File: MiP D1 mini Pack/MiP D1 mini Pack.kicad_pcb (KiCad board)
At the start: 2 copper layers, 41.4 x 63.8 mm, 12 parts, among them J1 MiP, J2 Debug, U1 WEMOS D1 mini

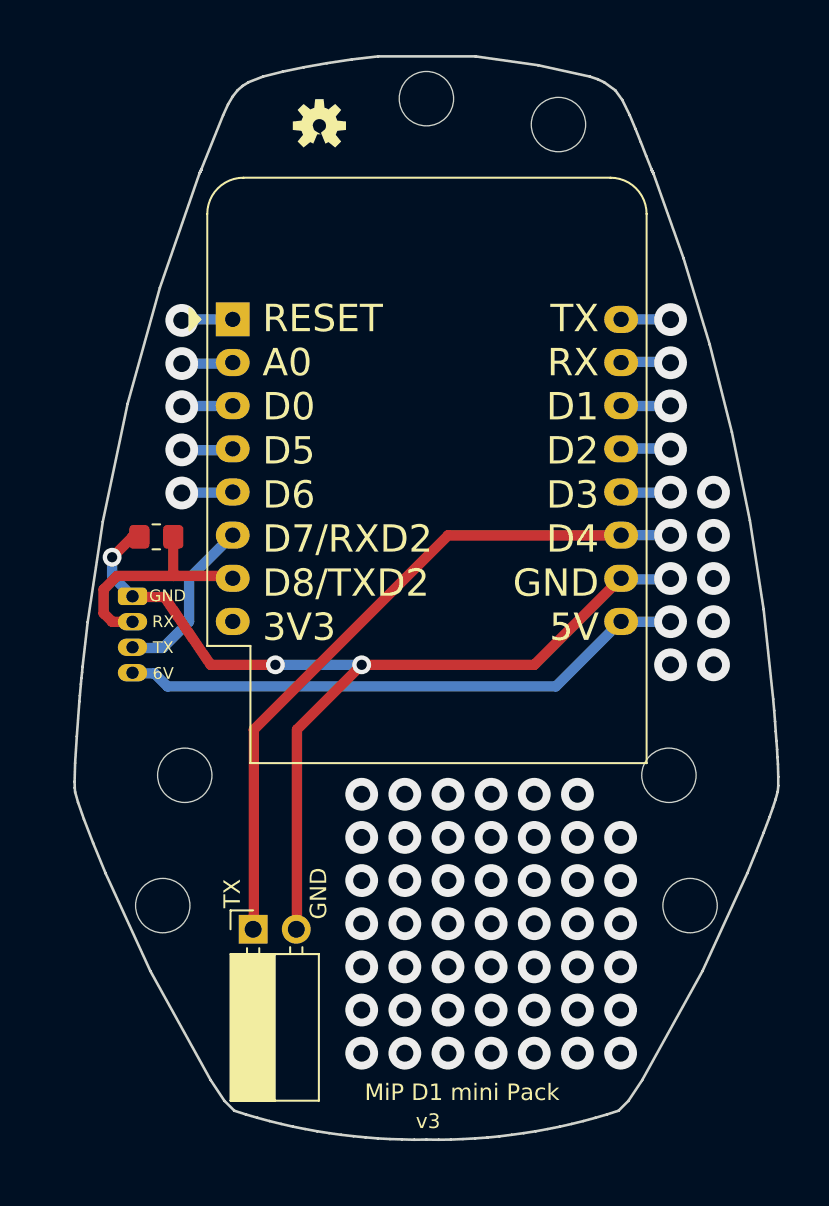
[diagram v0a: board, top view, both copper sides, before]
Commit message: Using tri-state buffer
Using tri-state buffer, not resistor, to decouple D1 mini from MiP.
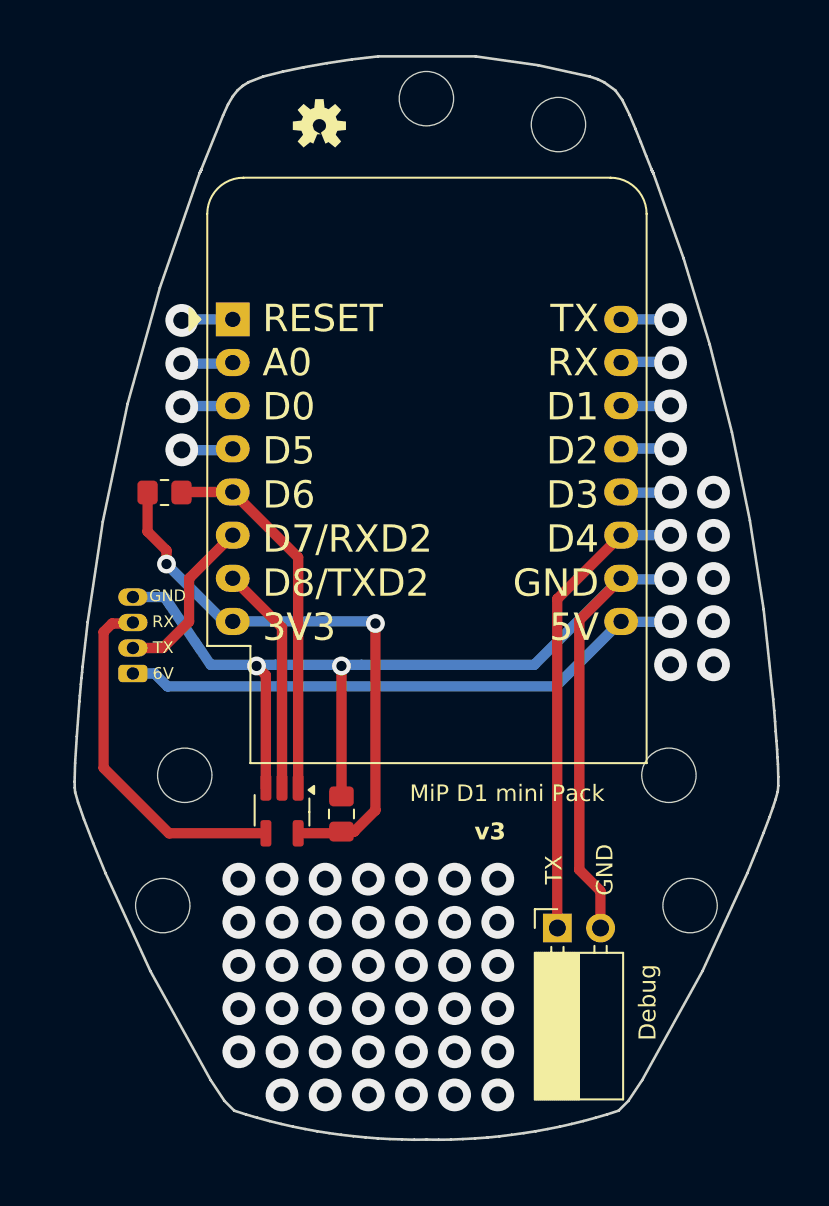
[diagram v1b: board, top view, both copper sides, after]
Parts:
- added C1: .1μF, Capacitor_SMD:C_0805_2012Metric_Pad1.18x1.45mm_HandSolder, F.Cu at (143.5, 117.7)
- added LOGO2: OSHW-LOGOS, OSHW-LOGO-S, B.Cu at (142.2, 77.2)
- added U2: 74LVC1G125, Package_TO_SOT_SMD:SOT-23-5_HandSoldering, F.Cu at (140.0, 117.5)
- R1: value 10kΩ -> 10K
- moved J2 17.9 mm to (156.2, 124.4)
- moved J1 4.54 mm to (131.2, 109.4), turned to 90 degrees
- moved R1 2.65 mm to (133.1, 98.8)
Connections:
- J1 pad 1: GND -> +6V
- J1 pad 2: /<NO NET> -> /RX
- J1 pad 3: /RX -> /BUF_TX
- J1 pad 4: +6V -> GND
- R1 pad 1: /<NO NET> -> Net-(U1-MISO/D6)
- R1 pad 2: GND -> +3V3
- U1 pad 5: unconnected-(U1-MISO/D6-Pad5) -> Net-(U1-MISO/D6)
- U1 pad 7: /<NO NET> -> /D1_TX
- U1 pad 8: unconnected-(U1-3V3-Pad8) -> +3V3
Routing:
- net +3V3: track 0.00 -> 34.5 mm, vias 0 -> 2
- net Net-(U1-MISO/D6): track 0.00 -> 22.0 mm
- net /BUF_TX: track 0.00 -> 21.1 mm
- net GND: track 58.1 -> 73.1 mm, vias 4 -> 3
- net /<NO NET>: track 14.0 -> 0.00 mm
- net /D1_TX: track 0.00 -> 13.8 mm
- net /Debug: track 41.2 -> 27.7 mm
- net unconnected-(U1-MISO/D6-Pad5): track 2.94 -> 0.00 mm, vias 1 -> 0
- net (no net): vias 54 -> 47

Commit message: Added planes
No, not flying planes.  Added voltage and ground planes.
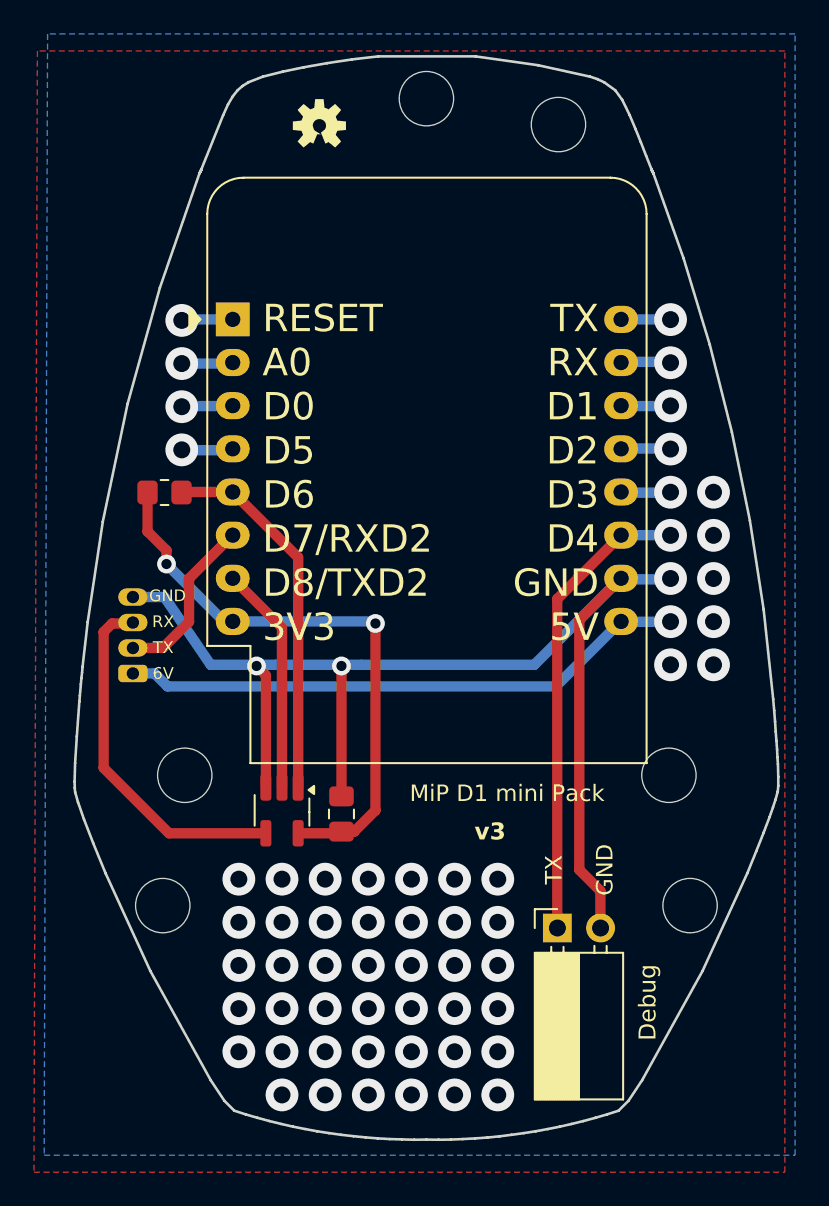
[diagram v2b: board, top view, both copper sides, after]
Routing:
- net GND: vias 3 -> 17
- net (no net): vias 47 -> 33
- added copper zone on F.Cu, net +6V
- added copper zone on B.Cu, net GND
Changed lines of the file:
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@@
-	)
-	(via
-		(at 165.4 103.8526)
-		(size 1.9304)
-		(drill 1)
-		(layers "F.Cu" "B.Cu")
-		(net "")
 	)
 	(via
@@
 	)
 	(via
-		(at 165.4 108.9326)
-		(size 1.9304)
-		(drill 1)
-		(layers "F.Cu" "B.Cu")
-		(net "")
-	)
-	(via
 		(at 137.46 131.71)
 		(size 1.9304)
@@
 	)
 	(via
-		(at 152.7 134.25)
-		(size 1.9304)
-		(drill 1)
-		(layers "F.Cu" "B.Cu")
-		(net "")
-	)
-	(via
 		(at 142.54 126.63)
 		(size 1.9304)
@@
 	)
 	(via
-		(at 152.7 124.09)
-		(size 1.9304)
-		(drill 1)
-		(layers "F.Cu" "B.Cu")
-		(net "")
-	)
-	(via
-		(at 145.08 121.55)
-		(size 1.9304)
-		(drill 1)
-		(layers "F.Cu" "B.Cu")
-		(net "")
-	)
-	(via
 		(at 145.08 124.09)
 		(size 1.9304)
@@
 	)
 	(via
-		(at 152.7 126.63)
-		(size 1.9304)
-		(drill 1)
-		(layers "F.Cu" "B.Cu")
-		(net "")
-	)
-	(via
 		(at 140 134.25)
 		(size 1.9304)
@@
 	)
 	(via
-		(at 152.7 121.55)
-		(size 1.9304)
-		(drill 1)
-		(layers "F.Cu" "B.Cu")
-		(net "")
-	)
-	(via
-		(at 142.54 121.55)
-		(size 1.9304)
-		(drill 1)
-		(layers "F.Cu" "B.Cu")
-		(net "")
-	)
-	(via
 		(at 137.46 129.17)
 		(size 1.9304)
@@
 	)
 	(via
-		(at 152.7 131.71)
-		(size 1.9304)
-		(drill 1)
-		(layers "F.Cu" "B.Cu")
-		(net "")
-	)
-	(via
 		(at 145.08 134.25)
 		(size 1.9304)
@@
 	)
 	(via
-		(at 165.4 101.3126)
-		(size 1.9304)
-		(drill 1)
-		(layers "F.Cu" "B.Cu")
-		(net "")
-	)
-	(via
 		(at 147.62 126.63)
 		(size 1.9304)
@@
 	)
 	(via
-		(at 150.16 121.55)
-		(size 1.9304)
-		(drill 1)
-		(layers "F.Cu" "B.Cu")
-		(net "")
-	)
-	(via
 		(at 145.08 126.63)
 		(size 1.9304)
@@
 	)
 	(via
-		(at 165.4 106.3926)
-		(size 1.9304)
-		(drill 1)
-		(layers "F.Cu" "B.Cu")
-		(net "")
-	)
-	(via
 		(at 147.62 134.25)
 		(size 1.9304)
@@
 	)
 	(via
-		(at 147.62 121.55)
-		(size 1.9304)
-		(drill 1)
-		(layers "F.Cu" "B.Cu")
-		(net "")
-	)
-	(via
 		(at 137.46 126.63)
 		(size 1.9304)
@@
 	(via
 		(at 137.46 124.09)
-		(size 1.9304)
-		(drill 1)
-		(layers "F.Cu" "B.Cu")
-		(net "")
-	)
-	(via
-		(at 152.7 129.17)
 		(size 1.9304)
 		(drill 1)
@@
 	)
 	(via
+		(at 165.4 103.8526)
+		(size 1.9304)
+		(drill 1)
+		(layers "F.Cu" "B.Cu")
+		(net "GND")
+	)
+	(via
+		(at 165.4 108.9326)
+		(size 1.9304)
+		(drill 1)
+		(layers "F.Cu" "B.Cu")
+		(net "GND")
+	)
+	(via
+		(at 152.7 134.25)
+		(size 1.9304)
+		(drill 1)
+		(layers "F.Cu" "B.Cu")
+		(net "GND")
+	)
+	(via
 		(at 138.5 109)
 		(size 1.108)
@@
 	)
 	(via
+		(at 152.7 124.09)
+		(size 1.9304)
+		(drill 1)
+		(layers "F.Cu" "B.Cu")
+		(net "GND")
+	)
+	(via
+		(at 145.08 121.55)
+		(size 1.9304)
+		(drill 1)
+		(layers "F.Cu" "B.Cu")
+		(net "GND")
+	)
+	(via
+		(at 152.7 126.63)
+		(size 1.9304)
+		(drill 1)
+		(layers "F.Cu" "B.Cu")
+		(net "GND")
+	)
+	(via
+		(at 152.7 121.55)
+		(size 1.9304)
+		(drill 1)
+		(layers "F.Cu" "B.Cu")
+		(net "GND")
+	)
+	(via
+		(at 142.54 121.55)
+		(size 1.9304)
+		(drill 1)
+		(layers "F.Cu" "B.Cu")
+		(net "GND")
+	)
+	(via
+		(at 152.7 131.71)
+		(size 1.9304)
+		(drill 1)
+		(layers "F.Cu" "B.Cu")
+		(net "GND")
+	)
+	(via
 		(at 143.5 109)
 		(size 1.108)
@@
 	)
 	(via
+		(at 165.4 101.3126)
+		(size 1.9304)
+		(drill 1)
+		(layers "F.Cu" "B.Cu")
+		(net "GND")
+	)
+	(via
+		(at 150.16 121.55)
+		(size 1.9304)
+		(drill 1)
+		(layers "F.Cu" "B.Cu")
+		(net "GND")
+	)
+	(via
+		(at 165.4 106.3926)
+		(size 1.9304)
+		(drill 1)
+		(layers "F.Cu" "B.Cu")
+		(net "GND")
+	)
+	(via
+		(at 147.62 121.55)
+		(size 1.9304)
+		(drill 1)
+		(layers "F.Cu" "B.Cu")
+		(net "GND")
+	)
+	(via
+		(at 152.7 129.17)
+		(size 1.9304)
+		(drill 1)
+		(layers "F.Cu" "B.Cu")
+		(net "GND")
+	)
+	(via
 		(at 162.8701 103.8526)
 		(size 1.9304)
@@
 		(net "unconnected-(U1-TX-Pad16)")
 	)
+	(zone
+		(net "+6V")
+		(layer "F.Cu")
+		(name "Voltage plane")
+		(hatch edge 0.5)
+		(connect_pads
+			(clearance 0.5)
+		)
+		(min_thickness 0.25)
+		(fill yes
+			(thermal_gap 0.5)
+			(thermal_bridge_width 0.5)
+			(island_removal_mode 0)
+		)
+		(polygon
+			(pts
+				(xy 125.6 72.8) (xy 125.4 138.8) (xy 169.6 138.8) (xy 169.6 72.8)
+			)
+		)
+	)
+	(zone
+		(net "GND")
+		(layer "B.Cu")
+		(name "Ground plane")
+		(hatch edge 0.5)
+		(connect_pads
+			(clearance 0.5)
+		)
+		(min_thickness 0.25)
+		(fill yes
+			(thermal_gap 0.5)
+			(thermal_bridge_width 0.5)
+			(island_removal_mode 0)
+		)
+		(polygon
+			(pts
+				(xy 126.2 71.8) (xy 126 137.8) (xy 170.2 137.8) (xy 170.2 71.8)
+			)
+		)
+	)
 	(embedded_fonts no)

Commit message: Corrected vias and planes
Some vias were connected to gthe ground plane,making them useless as a prototyping area.
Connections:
- C1 pad 2: GND -> (no net)
- J1 pad 4: GND -> (no net)
- J2 pad 2: GND -> (no net)
- U1 pad 10: GND -> (no net)
- U2 pad 3: GND -> (no net)
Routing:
- net GND: vias 17 -> 4
- net +6V: vias 1 -> 2
- net (no net): vias 33 -> 45
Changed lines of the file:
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@@
 			(layers "F.Cu" "F.Mask" "F.Paste")
 			(roundrect_rratio 0.212766)
-			(net "GND")
 			(pintype "passive")
 		)
@@
 			(layers "F.Cu" "F.Mask" "F.Paste")
 			(roundrect_rratio 0.25)
-			(net "GND")
 			(pinfunction "GND_3")
 			(pintype "power_in")
@@
 			(layers "*.Cu" "*.Mask")
 			(remove_unused_layers no)
-			(net "GND")
 			(pinfunction "Pin_2_2")
 			(pintype "passive")
@@
 			(layers "*.Cu" "*.Mask")
 			(remove_unused_layers no)
-			(net "GND")
 			(pinfunction "GND_10")
 			(pintype "power_in")
@@
 			(layers "*.Cu" "*.Mask")
 			(remove_unused_layers no)
-			(net "GND")
 			(pinfunction "Pin_4_4")
 			(pintype "power_out")
@@
 	)
 	(via
+		(at 165.4 108.9326)
+		(size 1.9304)
+		(drill 1)
+		(layers "F.Cu" "B.Cu")
+		(free yes)
+		(net "")
+	)
+	(via
 		(at 137.46 131.71)
 		(size 1.9304)
@@
 	)
 	(via
+		(at 152.7 134.25)
+		(size 1.9304)
+		(drill 1)
+		(layers "F.Cu" "B.Cu")
+		(free yes)
+		(net "")
+	)
+	(via
 		(at 142.54 126.63)
 		(size 1.9304)
@@
 	)
 	(via
+		(at 152.7 124.09)
+		(size 1.9304)
+		(drill 1)
+		(layers "F.Cu" "B.Cu")
+		(free yes)
+		(net "")
+	)
+	(via
+		(at 145.08 121.55)
+		(size 1.9304)
+		(drill 1)
+		(layers "F.Cu" "B.Cu")
+		(free yes)
+		(net "")
+	)
+	(via
 		(at 145.08 124.09)
 		(size 1.9304)
@@
 	)
 	(via
+		(at 152.7 126.63)
+		(size 1.9304)
+		(drill 1)
+		(layers "F.Cu" "B.Cu")
+		(free yes)
+		(net "")
+	)
+	(via
 		(at 140 134.25)
 		(size 1.9304)
@@
 	)
 	(via
+		(at 152.7 121.55)
+		(size 1.9304)
+		(drill 1)
+		(layers "F.Cu" "B.Cu")
+		(free yes)
+		(net "")
+	)
+	(via
+		(at 142.54 121.55)
+		(size 1.9304)
+		(drill 1)
+		(layers "F.Cu" "B.Cu")
+		(free yes)
+		(net "")
+	)
+	(via
 		(at 137.46 129.17)
 		(size 1.9304)
@@
 	)
 	(via
+		(at 152.7 131.71)
+		(size 1.9304)
+		(drill 1)
+		(layers "F.Cu" "B.Cu")
+		(free yes)
+		(net "")
+	)
+	(via
 		(at 145.08 134.25)
 		(size 1.9304)
@@
 	)
 	(via
+		(at 165.4 101.3126)
+		(size 1.9304)
+		(drill 1)
+		(layers "F.Cu" "B.Cu")
+		(free yes)
+		(net "")
+	)
+	(via
 		(at 147.62 126.63)
 		(size 1.9304)
@@
 	)
 	(via
+		(at 150.16 121.55)
+		(size 1.9304)
+		(drill 1)
+		(layers "F.Cu" "B.Cu")
+		(free yes)
+		(net "")
+	)
+	(via
 		(at 145.08 126.63)
 		(size 1.9304)
@@
 	)
 	(via
+		(at 147.62 121.55)
+		(size 1.9304)
+		(drill 1)
+		(layers "F.Cu" "B.Cu")
+		(free yes)
+		(net "")
+	)
+	(via
 		(at 137.46 126.63)
 		(size 1.9304)
@@
 	)
 	(via
+		(at 152.7 129.17)
+		(size 1.9304)
+		(drill 1)
+		(layers "F.Cu" "B.Cu")
+		(free yes)
+		(net "")
+	)
+	(via
 		(at 142.54 134.25)
 		(size 1.9304)
@@
 	)
 	(via
-		(at 165.4 108.9326)
-		(size 1.9304)
-		(drill 1)
-		(layers "F.Cu" "B.Cu")
-		(net "GND")
-	)
-	(via
-		(at 152.7 134.25)
-		(size 1.9304)
-		(drill 1)
-		(layers "F.Cu" "B.Cu")
-		(net "GND")
-	)
-	(via
 		(at 138.5 109)
 		(size 1.108)
@@
 	)
 	(via
-		(at 152.7 124.09)
-		(size 1.9304)
-		(drill 1)
-		(layers "F.Cu" "B.Cu")
-		(net "GND")
-	)
-	(via
-		(at 145.08 121.55)
-		(size 1.9304)
-		(drill 1)
-		(layers "F.Cu" "B.Cu")
-		(net "GND")
-	)
-	(via
-		(at 152.7 126.63)
-		(size 1.9304)
-		(drill 1)
-		(layers "F.Cu" "B.Cu")
-		(net "GND")
-	)
-	(via
-		(at 152.7 121.55)
-		(size 1.9304)
-		(drill 1)
-		(layers "F.Cu" "B.Cu")
-		(net "GND")
-	)
-	(via
-		(at 142.54 121.55)
-		(size 1.9304)
-		(drill 1)
-		(layers "F.Cu" "B.Cu")
-		(net "GND")
-	)
-	(via
-		(at 152.7 131.71)
-		(size 1.9304)
-		(drill 1)
-		(layers "F.Cu" "B.Cu")
-		(net "GND")
-	)
-	(via
 		(at 143.5 109)
 		(size 1.108)
@@
 	)
 	(via
-		(at 165.4 101.3126)
-		(size 1.9304)
-		(drill 1)
-		(layers "F.Cu" "B.Cu")
-		(net "GND")
-	)
-	(via
-		(at 150.16 121.55)
-		(size 1.9304)
-		(drill 1)
-		(layers "F.Cu" "B.Cu")
-		(net "GND")
-	)
-	(via
-		(at 165.4 106.3926)
-		(size 1.9304)
-		(drill 1)
-		(layers "F.Cu" "B.Cu")
-		(net "GND")
-	)
-	(via
-		(at 147.62 121.55)
-		(size 1.9304)
-		(drill 1)
-		(layers "F.Cu" "B.Cu")
-		(net "GND")
-	)
-	(via
-		(at 152.7 129.17)
-		(size 1.9304)
-		(drill 1)
-		(layers "F.Cu" "B.Cu")
-		(net "GND")
-	)
-	(via
 		(at 162.8701 103.8526)
 		(size 1.9304)
@@
 	)
 	(via
+		(at 165.4 106.3926)
+		(size 1.9304)
+		(drill 1)
+		(layers "F.Cu" "B.Cu")
+		(free yes)
+		(net "+6V")
+	)
+	(via
